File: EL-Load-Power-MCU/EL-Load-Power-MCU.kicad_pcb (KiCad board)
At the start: 4 copper layers, 185 x 72.5 mm, 129 parts, among them J1 Conn_01x02, J10 Power for serial interface, J11 Conn_02x08_Odd_Even, J12 Conn_01x05_Pin, J2 Conn_01x02, J3 Touchscreen, J4 JST-S6B-PH-SM4, J5 PN sensor, J6 PN sensor, J7 Conn_02x08_Odd_Even, J8 Conn_02x06_Odd_Even, J9 SWD+UART header, M1 Fan_4pin, M2 Fan_4pin, M3 Fan_4pin, Q1 BSS138, Q2 BSS138, SW1 Pico Reset, T1 Wuerth_750316031, T2 Wuerth_750316031, U1 MAX31760, U10 MC34063AD, U11 24C64, U2 SN6505BDBV, U3 MAX31760, U4 Si8602AB, U5 AMS1117-3.3, U6 MCP23017_SO, U7 AZ1117-5.0, U8 SC0915, U9 AMS1117-3.3

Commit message: Working on #4,#2 fixed #8,#22
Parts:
- D16: value 16V -> 20V
- Q1, Q2: value BSS138 -> BSS138W; footprint Package_TO_SOT_SMD:SOT-23 -> Package_TO_SOT_SMD:SOT-323_SC-70
- T1: value Wuerth_750316031 -> Wuerth_750315371
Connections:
- U6 pad 21: /MCU/~{VonLatch} -> /MCU/~{Von}
- U6 pad 28: /MCU/~{Von} -> /MCU/~{VonLatch}
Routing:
- net /MCU/~{Von}: track 68.1 -> 59.0 mm
- net /MCU/~{VonLatch}: track 28.5 -> 19.5 mm
- net +3V3: track 298.0 -> 297.4 mm
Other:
- board text added: "${TITLE} v${REVISION} ${ISSUE_DATE}"
- board text removed: "${TITLE} v${REVISION} ${CURRENT_DATE}"

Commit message: EL-Load-Power-MCU PCB v4r4 release.
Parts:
- removed D11: SS14, Diode_SMD:D_SMA
- removed J3: Touchscreen, Connector_PinSocket_2.54mm:PinSocket_1x11_P2.54mm_Vertical
- removed J4: JST-S6B-PH-SM4, Connector_JST:JST_PH_S6B-PH-SM4-TB_1x06-1MP_P2.00mm_Horizontal
- removed J6: PN sensor, Connector_PinHeader_2.54mm:PinHeader_1x02_P2.54mm_Vertical
- removed M3: Fan_4pin, Connector:FanPinHeader_1x04_P2.54mm_Vertical
- removed kibuzzard-6569E6D8: G***, kibuzzard-6569E6D8
- removed kibuzzard-658AD76B: G***, kibuzzard-658AD76B
- added BZ1: Buzzer, Buzzer_Beeper:Buzzer_12x9.5RM7.6, F.Cu at (172.1, 79.1)
- added C29: 1u, Capacitor_SMD:C_0805_2012Metric, F.Cu at (196.0, 61.5)
- added C31: 100n, Capacitor_SMD:C_0805_2012Metric, F.Cu at (196.0, 63.6)
- added C32: 10u, Capacitor_SMD:CP_Elec_5x5.8, F.Cu at (197.8, 67.8)
- added JP11: HW V3/V4, Connector_PinHeader_2.54mm:PinHeader_1x02_P2.54mm_Vertical, F.Cu at (162.3, 79.1)
- added JP12: LDO En, Connector_PinHeader_2.54mm:PinHeader_1x02_P2.54mm_Vertical, F.Cu at (53.4, 54.0)
- added Q3: BSS138W, Package_TO_SOT_SMD:SOT-323_SC-70, F.Cu at (190.3, 78.3)
- added R26: 3k, Resistor_SMD:R_0805_2012Metric, F.Cu at (194.2, 29.3)
- added R27: 3k, Resistor_SMD:R_0805_2012Metric, F.Cu at (197.6, 29.3)
- added R28: 10k, Resistor_SMD:R_0805_2012Metric, F.Cu at (54.3, 49.6)
- added R29: 1k, Resistor_SMD:R_0805_2012Metric, F.Cu at (185.4, 77.3)
- added R30: 1k, Resistor_SMD:R_0805_2012Metric, F.Cu at (168.1, 80.1)
- added R31: 20k, Resistor_SMD:R_0805_2012Metric, F.Cu at (191.1, 74.1)
- added kibuzzard-66FFF99B: G***, kibuzzard-66FFF99B, F.Cu at (132.5, 48.5)
- C1, C13, C19, C30, C4, C6, C7: footprint Capacitor_SMD:CP_Elec_6.3x5.8 -> Capacitor_SMD:CP_Elec_5x5.8
- C12: value 100n -> 2.2u
- C14: value 10u -> 1u; footprint Capacitor_SMD:CP_Elec_6.3x5.8 -> Capacitor_SMD:C_0805_2012Metric
- C15: value 100n -> 10u; footprint Capacitor_SMD:C_0805_2012Metric -> Capacitor_SMD:CP_Elec_5x5.8
- C18, C20, C22, C23: footprint Capacitor_SMD:C_0805_2012Metric -> Capacitor_SMD:CP_Elec_5x5.8
- C27: value 200n -> 200p
- D17: value 1N5819WS -> SS14
- J11: value Conn_02x08_Odd_Even -> IDC-Header 2x08 P2.54mm
- J12: footprint Connector_PinHeader_2.54mm:PinHeader_1x05_P2.54mm_Vertical -> Connector_PinHeader_2.54mm:PinHeader_1x03_P2.54mm_Vertical
- J7: value Conn_02x08_Odd_Even -> PinHeader 2x08 P2.54mm; footprint Connector_PinSocket_2.54mm:PinSocket_2x08_P2.54mm_Vertical -> Connector_PinHeader_2.54mm:PinHeader_2x08_P2.54mm_Vertical
- J8: value Conn_02x06_Odd_Even -> PinHeader 2x08 P2.54mm
- JP3: value I2C Address -> Fan Volt/PWM; footprint Jumper:SolderJumper-3_P1.3mm_Bridged2Bar12_RoundedPad1.0x1.5mm -> Connector_PinHeader_2.54mm:PinHeader_1x03_P2.54mm_Vertical
- R1, R2, R22, R3, R5: footprint Resistor_SMD:R_0805_2012Metric_Pad1.20x1.40mm_HandSolder -> Resistor_SMD:R_0805_2012Metric
- R10: value 10 -> 3k3; footprint Resistor_SMD:R_0805_2012Metric_Pad1.20x1.40mm_HandSolder -> Resistor_SMD:R_0805_2012Metric
- R11: value 1k -> 3k3; footprint Resistor_SMD:R_0805_2012Metric_Pad1.20x1.40mm_HandSolder -> Resistor_SMD:R_0805_2012Metric
- R6: value 4k7 -> 10; footprint Resistor_SMD:R_0805_2012Metric_Pad1.20x1.40mm_HandSolder -> Resistor_SMD:R_0805_2012Metric
- R7: value 4k7 -> 1k; footprint Resistor_SMD:R_0805_2012Metric_Pad1.20x1.40mm_HandSolder -> Resistor_SMD:R_0805_2012Metric
- R8: value 10 -> 1k; footprint Resistor_SMD:R_0805_2012Metric_Pad1.20x1.40mm_HandSolder -> Resistor_SMD:R_0805_2012Metric
- R9: value 1k -> 39k; footprint Resistor_SMD:R_0805_2012Metric_Pad1.20x1.40mm_HandSolder -> Resistor_SMD:R_0805_2012Metric
- TP5: value GND -> TestPoint_Probe
- U3: value MAX31760 -> BD00FC0WFP-E2; footprint Package_SO:QSOP-16_3.9x4.9mm_P0.635mm -> Package_TO_SOT_SMD:TO-252-5_TabPin6
- moved SW1 50.2 mm to (162.2, 36.8), turned to 180 degrees
- moved C10 32.3 mm to (54.8, 66.7)
- moved D10 30.3 mm to (57.5, 83.1)
- moved C23 29.4 mm to (124.2, 29.3)
- moved D17 29.4 mm to (50.6, 40.0), turned to 90 degrees
- moved D5 28.8 mm to (46.4, 83.0), turned to 180 degrees
- moved C20 28.2 mm to (110.2, 29.3)
- moved C26 27.9 mm to (69.3, 26.8), turned to 180 degrees
- moved R6 26.4 mm to (51.4, 69.5)
- moved R8 25.3 mm to (50.8, 64.3)
- moved U3 23.6 mm to (51.8, 59.6), turned to 0 degrees
- moved U9 23.5 mm to (124.0, 36.9)
- moved J2 23.3 mm to (32.0, 65.2)
- moved C24 22.7 mm to (118.2, 40.1), turned to 0 degrees
- moved J10 22.5 mm to (133.2, 37.5)
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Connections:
- net Net-(M1-Tacho) renamed /Fan Controllers/Fan1Tacho
- net Net-(U8-GP14) renamed /MCU/HWGPIO_INT
- C10 pad 1: +3V3_ISO -> Net-(U1-TACH2)
- C12 pad 1: Net-(U3-TACH1) -> +V_FANS
- C14 pad 1: +V_FANS -> Net-(C14-Pad1)
- C15 pad 1: Net-(U3-TACH2) -> /Fan Controllers/Fan1PWR
- C18 pad 1: GND_ISO -> +V_FANS
- C18 pad 2: +V_FANS -> GND_ISO
- C20 pad 1: GND -> +7VU
- C20 pad 2: +7VU -> GND
- C22 pad 1: GND -> +5VD
- C22 pad 2: +5VD -> GND
- C23 pad 1: GND -> +7VU
- C23 pad 2: +7VU -> GND
- D10 pad 1: +V_FANS -> /Fan Controllers/Fan1PWR
- D5 pad 1: +V_FANS -> /Fan Controllers/Fan1PWR
- J1 pad 2: Net-(J1-Pin_2) -> GND_ISO
- J11 pad 12: /SDA -> /_KEYS_SDA
- J11 pad 13: /SCL -> /_KEYS_SCL
- J2 pad 1: +12V_ISO -> Net-(J2-Pin_1)
- J2 pad 2: GND_ISO -> Net-(J2-Pin_2)
- J7 pad 1: /MCU/OCPtriggered -> /MCU/resetProt
- J7 pad 10: /MCU/EL-ADC_CLK -> /MCU/EL-SPI_RX
- J7 pad 11: /MCU/EL-DAC1_CS -> GND
- J7 pad 12: GND -> /MCU/EL-DAC1_CS
- J7 pad 13: /MCU/currRangeLow -> +3V3
- J7 pad 14: +3V3 -> /MCU/currRangeLow
- J7 pad 15: /MCU/~{Von} -> /MCU/EL-DAC2_CS
- J7 pad 16: /MCU/EL-DAC2_CS -> /MCU/~{Von}
- J7 pad 2: /MCU/resetProt -> /MCU/OCPtriggered
- J7 pad 3: /MCU/OVPtriggered -> /MCU/clampOff
- J7 pad 4: /MCU/clampOff -> /MCU/OVPtriggered
- J7 pad 5: /MCU/EL-ADC_CS -> /MCU/EL-ADC_RDY
- J7 pad 6: /MCU/EL-DAC_RDY -> /MCU/EL-ADC_CS
- J7 pad 7: /MCU/EL-SPI_SCK -> /MCU/EL-SPI_TX
- J7 pad 8: /MCU/EL-SPI_TX -> /MCU/EL-SPI_SCK
- J7 pad 9: /MCU/EL-SPI_RX -> /MCU/EL-ADC_CLK
- J8 pad 8: +15VU -> /_reversePolarity
- J9 pad 1: unconnected-(J9-Pin_1-Pad1) -> +3V3
- JP10 pad 1: Net-(JP10-A) -> Net-(J1-Pin_1)
- JP3 pad 1: +3V3_ISO -> Net-(JP3-A)
- JP3 pad 2: Net-(JP3-C) -> /Fan Controllers/Fan1PWR
- JP3 pad 3: GND_ISO -> +V_FANS
- L1 pad 1: Net-(J1-Pin_1) -> Net-(J2-Pin_2)
- L1 pad 2: Net-(J1-Pin_2) -> Net-(J2-Pin_1)
- L1 pad 3: GND_ISO -> +12V_ISO
- L1 pad 4: Net-(JP10-A) -> GND_ISO
- M1 pad 2: +V_FANS -> /Fan Controllers/Fan1PWR
- M1 pad 4: Net-(M1-PWM) -> /Fan Controllers/Fan1PWM
- M2 pad 2: +V_FANS -> /Fan Controllers/Fan1PWR
- M2 pad 3: Net-(M2-Tacho) -> /Fan Controllers/Fan2Tacho
- M2 pad 4: Net-(M2-PWM) -> /Fan Controllers/Fan1PWM
- Q1 pad 2: /SDA -> /MCU/HWIO_SDA
- Q2 pad 2: /SCL -> /MCU/HWIO_SCL
- R10 pad 1: Net-(U3-TACH2) -> Net-(U3-FB)
- R10 pad 2: Net-(M3-Tacho) -> GND_ISO
- R11 pad 1: +3V3_ISO -> Net-(U3-FB)
- R11 pad 2: Net-(M3-Tacho) -> Net-(C14-Pad1)
- R15 pad 2: /SCL -> /MCU/HWIO_SCL
- R16 pad 2: /SDA -> /MCU/HWIO_SDA
- R2 pad 2: Net-(M1-PWM) -> /Fan Controllers/Fan1PWM
- R6 pad 1: Net-(U3-~{SHDN}) -> Net-(U1-TACH2)
- R6 pad 2: +3V3_ISO -> /Fan Controllers/Fan2Tacho
- R7 pad 2: Net-(M2-PWM) -> /Fan Controllers/Fan2Tacho
- R8 pad 1: Net-(U3-TACH1) -> /Fan Controllers/Fan1PWM
- R8 pad 2: Net-(M2-Tacho) -> Net-(C14-Pad1)
- R9 pad 1: +3V3_ISO -> Net-(JP3-A)
- R9 pad 2: Net-(M2-Tacho) -> Net-(U3-FB)
- U1 pad 6: Net-(M1-PWM) -> /Fan Controllers/Fan1PWM
- U1 pad 9: unconnected-(U1-TACH2-Pad9) -> Net-(U1-TACH2)
- U11 pad 5: /SDA -> /MCU/HWIO_SDA
- U11 pad 6: /SCL -> /MCU/HWIO_SCL
- U3 pad 1: /Fan Controllers/DXP -> Net-(JP12-A)
- U3 pad 2: /Fan Controllers/DXN -> +V_FANS
- U3 pad 3: GND_ISO -> unconnected-(U3-N.C.-Pad3)
- U3 pad 4: Net-(JP3-C) -> Net-(JP3-A)
- U3 pad 5: GND_ISO -> Net-(U3-FB)
- U3 pad 6: Net-(M2-PWM) -> GND_ISO
- U4 pad 2: /SDA -> /MCU/HWIO_SDA
- U4 pad 3: /SCL -> /MCU/HWIO_SCL
- U6 pad 28: /MCU/~{VonLatch} -> /MCU/reversePolarity
- U6 pad 3: Net-(J12-Pin_4) -> /MCU/Buzzer
- U6 pad 4: Net-(J12-Pin_5) -> /MCU/VoltSenseClear
- U6 pad 5: /MCU/VoltSenseClear -> /MCU/~{VonLatch}
- U8 pad 10: /MCU/EL-DAC_RDY -> /MCU/EL-ADC_RDY
- U8 pad 21: /CS2 -> /_KEYS_SDA
- U8 pad 22: /PEN -> /_KEYS_SCL
- U8 pad 24: /~{RESET} -> /CS2
- U8 pad 25: unconnected-(U8-GP19-Pad25) -> /~{RESET}
- U8 pad 26: /MCU/EL-ADC_CS -> /PEN
- U8 pad 29: unconnected-(U8-GP22-Pad29) -> /MCU/EL-ADC_CS
- U8 pad 31: /SDA -> /MCU/HWIO_SDA
- U8 pad 32: /SCL -> /MCU/HWIO_SCL
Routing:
- net /SDA: track 164.3 -> 0.00 mm, vias 5 -> 0
- net /SCL: track 153.7 -> 0.00 mm, vias 4 -> 0
- net /MCU/HWIO_SDA: track 0.00 -> 127.4 mm, vias 0 -> 3
- net /MCU/HWIO_SCL: track 0.00 -> 108.7 mm, vias 0 -> 3
- net /MCU/EL-DAC_RDY: track 95.5 -> 0.00 mm, vias 1 -> 0
- net /MCU/EL-ADC_RDY: track 0.00 -> 94.5 mm, vias 0 -> 1
- net /MCU/Buzzer: track 0.00 -> 82.2 mm, vias 0 -> 2
- net Net-(J1-Pin_1): track 13.3 -> 74.6 mm
- net Net-(JP10-A): track 57.8 -> 0.00 mm, vias 1 -> 0
- net +5VD: track 140.1 -> 196.0 mm, vias 5 -> 6
- net /Fan Controllers/Fan1PWR: track 0.00 -> 55.4 mm
- net +V_FANS: track 109.2 -> 62.5 mm
- net Net-(U8-~{RUN}): track 66.1 -> 19.4 mm, vias 2 -> 0
- net /Fan Controllers/Fan1PWM: track 0.00 -> 43.7 mm, vias 0 -> 1
- net +3V3_ISO: track 159.3 -> 118.0 mm
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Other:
- board size 185 x 72.5 mm -> 179 x 72.5 mm
- board text added: "+7VUuf"
- board text added: "-7VUuf"
- board text added: "3V3 TX RX SWDIO GND SWCLK"
- board text added: "LDO Enable"
- board text added: "Var Vfan Fixed"
- board text removed: "- TX RX SWDIO GND SWCLK"
- board text removed: "~{RESET} INT SCL SDA GND 3V3"

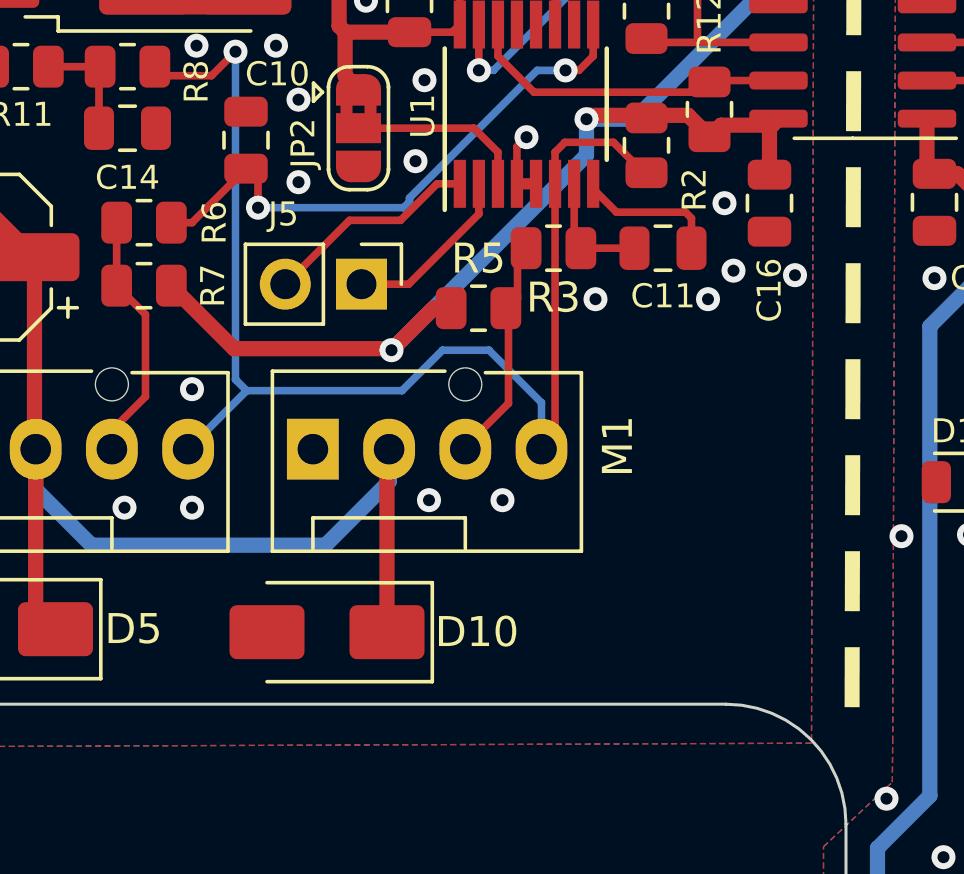
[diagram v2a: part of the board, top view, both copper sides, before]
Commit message: Fixed fan driver with jumper. Initial v5 version (still KiCad7)
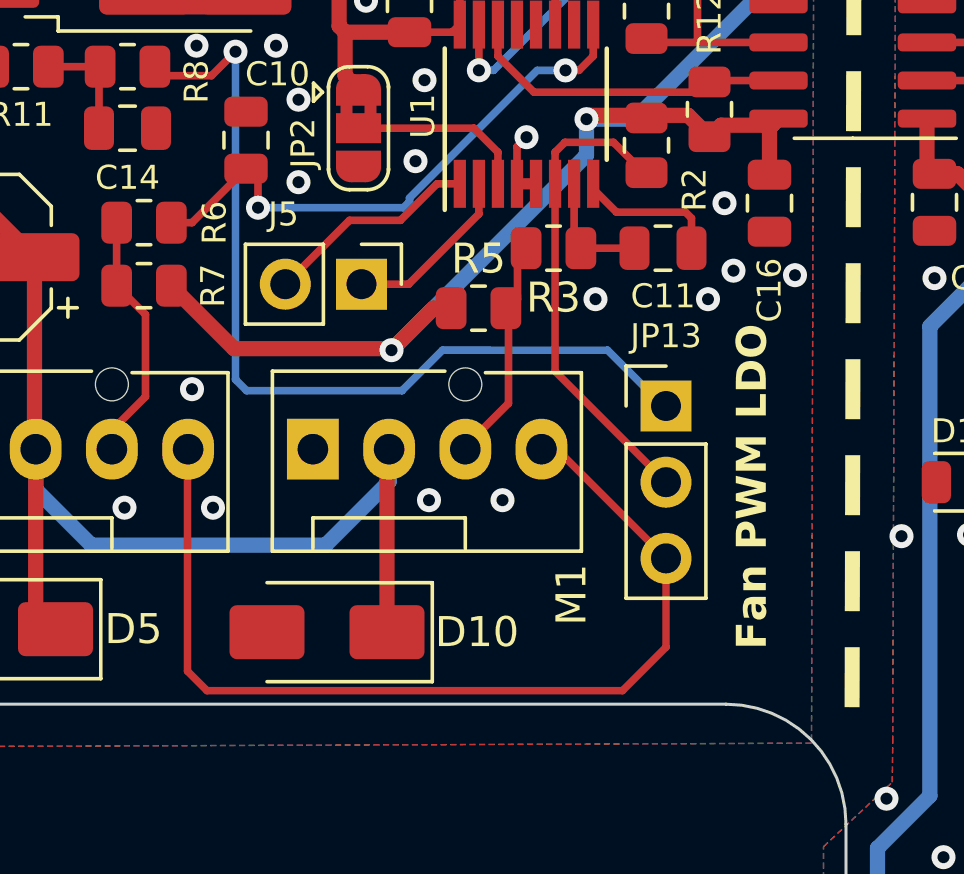
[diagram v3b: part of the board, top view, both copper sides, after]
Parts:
- added JP13: PWM 2 LDO/PWM, Connector_PinHeader_2.54mm:PinHeader_1x03_P2.54mm_Vertical, F.Cu at (68.8, 75.6)
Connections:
- R2 pad 2: /Fan Controllers/Fan1PWM -> Net-(JP13-C)
- R8 pad 1: /Fan Controllers/Fan1PWM -> Net-(JP13-A)
- U1 pad 6: /Fan Controllers/Fan1PWM -> Net-(JP13-C)
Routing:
- net Net-(JP13-A): track 0.00 -> 29.9 mm, vias 0 -> 1
- net Net-(JP13-C): track 0.00 -> 16.2 mm
- net /Fan Controllers/Fan1PWM: track 43.7 -> 33.5 mm, vias 1 -> 0
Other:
- board text added: "Fan PWM LDO"
